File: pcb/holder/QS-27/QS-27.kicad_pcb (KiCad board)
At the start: 2 copper layers, 20.8 x 20.6 mm, 2 parts, among them J1 Nixie_Conn_12P

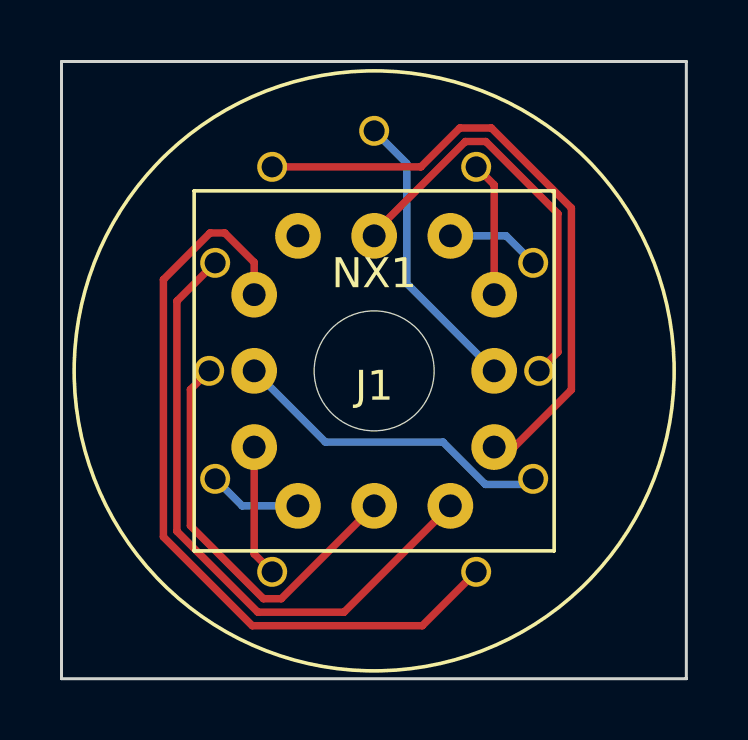
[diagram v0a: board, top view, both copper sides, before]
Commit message: Fix typo on nixie segment
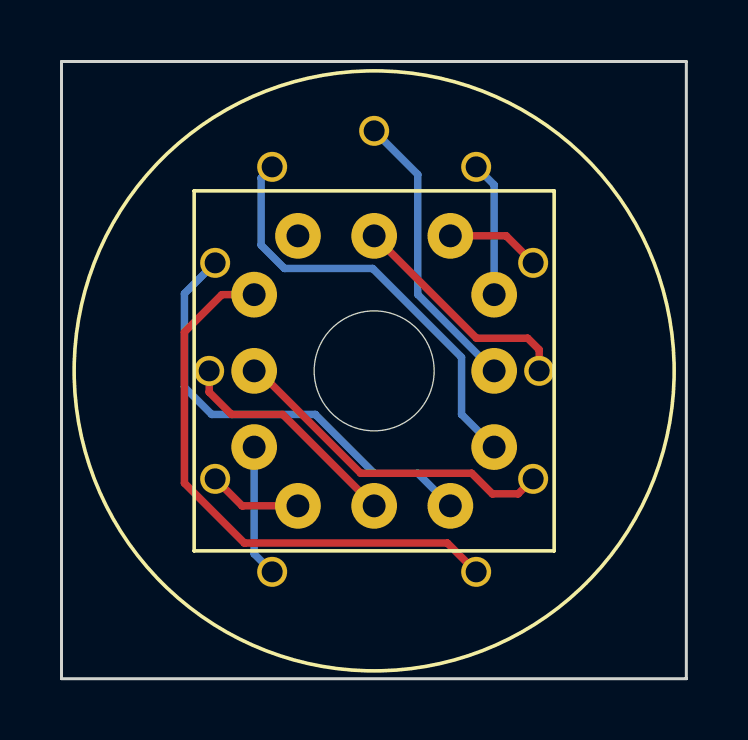
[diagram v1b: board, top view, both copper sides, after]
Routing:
- net PA: track 26.1 -> 18.8 mm
- net P5: track 21.0 -> 14.4 mm
- net P9: track 14.0 -> 7.78 mm
- net P4: track 21.2 -> 15.1 mm
- net P3: track 13.8 -> 7.78 mm

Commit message: Ver 3.0
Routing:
- net P5: track 14.4 -> 20.7 mm
- net P3: track 7.78 -> 13.6 mm
- net P4: track 15.1 -> 20.6 mm
- net P9: track 7.78 -> 11.6 mm
- net P7: track 4.51 -> 6.97 mm
- net P1: track 4.41 -> 6.87 mm
- net PA: track 18.8 -> 20.6 mm
